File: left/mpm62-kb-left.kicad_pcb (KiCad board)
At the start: 2 copper layers, 138.1 x 95.2 mm, 65 parts, among them J1 Conn_01x04_Male, SW1 SW_Push, U1 ProMicro

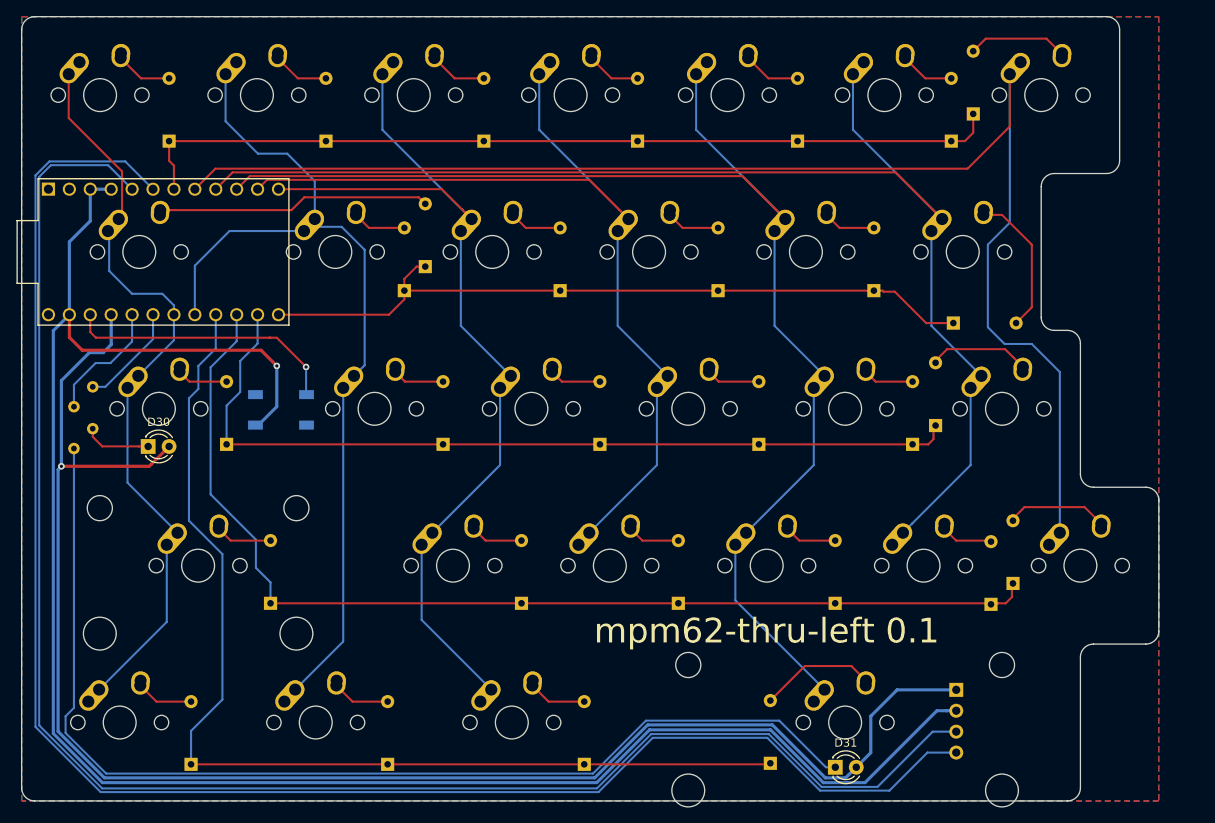
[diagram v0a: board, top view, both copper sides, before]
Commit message: Fix issues with left side: 1. SCL and SDA are swapped in the library file from github/ProMicroKiCad. Current fix is to swap the wires and mark the schematic to show which is which. Ultimately it would be good to get an updated lib file, but there is a PR for this which has never been accepted. 2. Was missing pullup resistors for I2C bus. 3. Resistor sizes on PCB were smaller than typical TH resistors. 4. Added extra header for power and ground to ease debugging.
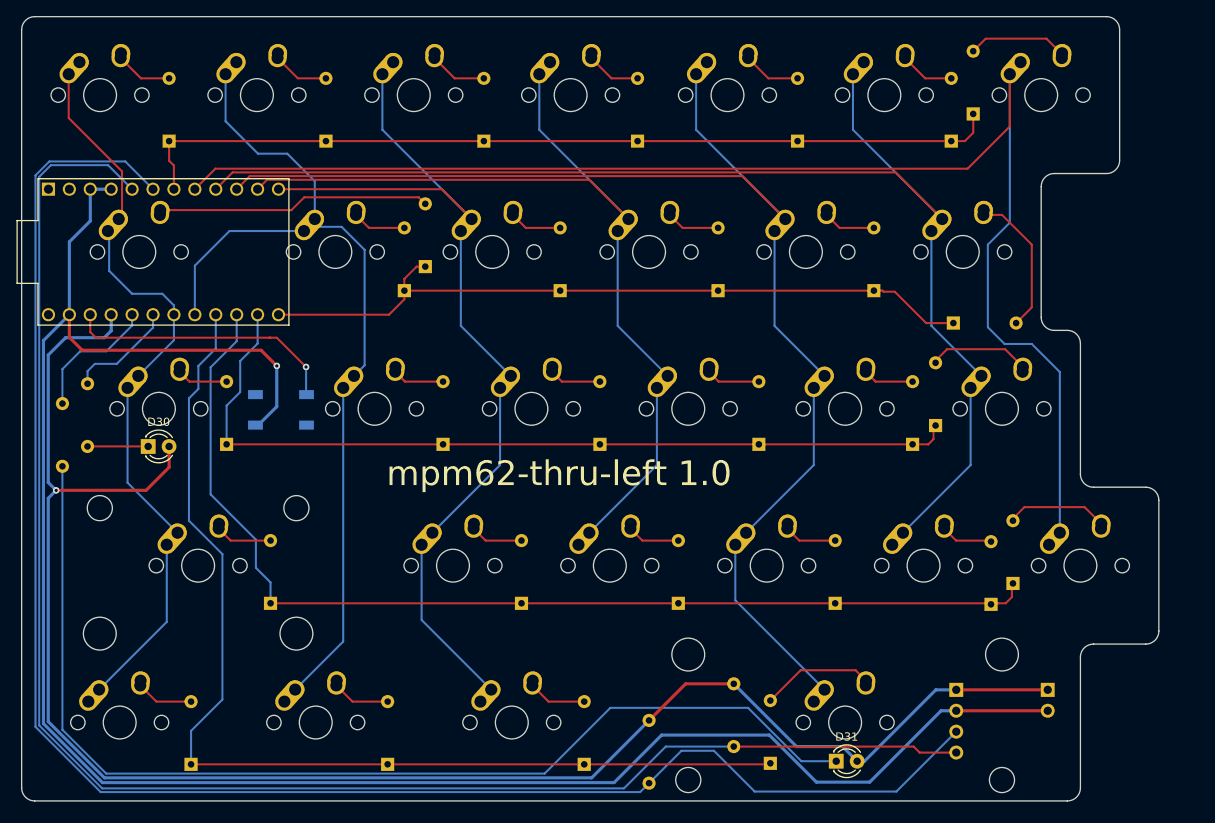
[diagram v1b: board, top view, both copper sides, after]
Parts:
- added J2: Conn_01x02_Male, Connector_PinHeader_2.54mm:PinHeader_1x02_P2.54mm_Vertical, B.Cu at (204.0, 113.5)
- added R3: 2.2K, Resistor_THT:R_Axial_DIN0207_L6.3mm_D2.5mm_P7.62mm_Horizontal, B.Cu at (165.9, 112.8)
- added R4: 2.2K, Resistor_THT:R_Axial_DIN0207_L6.3mm_D2.5mm_P7.62mm_Horizontal, B.Cu at (155.6, 117.2)
- MX23: footprint MX_Alps_Hybrid:MX-3U-NoLED -> MX_Alps_Hybrid:MX-3U-ReversedStabilizers-NoLED
- R1, R2: value R_Small -> 100; footprint Resistor_THT:R_Axial_DIN0204_L3.6mm_D1.6mm_P5.08mm_Horizontal -> Resistor_THT:R_Axial_DIN0207_L6.3mm_D2.5mm_P7.62mm_Horizontal
- moved R2 2.57 mm to (84.3, 86.4)
- moved R1 2.25 mm to (87.4, 83.9)
- moved D31 0.74 mm to (178.3, 122.2)
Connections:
- U1 pad 5: Net-(J1-Pad3) -> Net-(J1-Pad4)
- U1 pad 6: Net-(J1-Pad4) -> Net-(J1-Pad3)
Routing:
- net VCC: track 192.1 -> 210.0 mm
- net GND: track 229.4 -> 240.9 mm
- net Net-(J1-Pad4): track 205.8 -> 197.2 mm
- net Net-(J1-Pad3): track 202.4 -> 205.6 mm
- net Net-(D31-Pad1): track 135.5 -> 134.2 mm
- net Net-(R2-Pad2): track 15.2 -> 16.2 mm
- net Net-(D30-Pad1): track 8.21 -> 7.37 mm
- net Net-(R1-Pad2): track 12.7 -> 13.2 mm
- removed copper zone on B.Cu, net GND
- removed copper zone on F.Cu, net GND
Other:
- board text added: "mpm62-thru-left 1.0"
- board text removed: "mpm62-thru-left 0.1"

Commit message: Final for b1t (board 1 thruhole) board
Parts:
- added G***: LOGO, MpmMisc:small_logo, B.Cu at (121.4, 108.7)
- added G***: LOGO, MpmMisc:biglogo3, F.Cu at (144.4, 73.9)
- added H1: MountingHole, MountingHole:MountingHole_2.2mm_M2_Pad, F.Cu at (105.6, 60.3)
- added H2: MountingHole, MountingHole:MountingHole_2.2mm_M2_Pad, F.Cu at (103.2, 117.5)
- added H3: MountingHole, MountingHole:MountingHole_2.2mm_M2_Pad, F.Cu at (193.7, 50.8)
- added H4: MountingHole, MountingHole:MountingHole_2.2mm_M2_Pad, F.Cu at (192.9, 110.3)
- added U2: TRRS, Keebio-Parts:TRRS-PJ-320A, B.Cu at (204.3, 113.7)
- J1: value Conn_01x04_Male -> Raw Header
- J2: value Conn_01x02_Male -> JST ZH header; footprint Connector_PinHeader_2.54mm:PinHeader_1x02_P2.54mm_Vertical -> MpmMisc:JST_ZH_B4B-ZR_1x04_P1.50mm_Vertical
- MX1, MX10, MX11, MX12, MX13, MX15, MX16, MX17, MX18, MX19, MX20, MX21, MX22, MX24, MX25, MX26, MX27, MX28, MX29, MX6, MX7, MX8: footprint MX_Alps_Hybrid:MX-1U-NoLED -> MX_Only:MXOnly-1U-NoLED
- MX14, MX5, MX9: footprint MX_Alps_Hybrid:MX-1.25U-NoLED -> MX_Only:MXOnly-1.25U-NoLED
- MX2: footprint MX_Alps_Hybrid:MX-1.5U-NoLED -> MX_Only:MXOnly-1.5U-NoLED
- MX23: footprint MX_Alps_Hybrid:MX-3U-ReversedStabilizers-NoLED -> MX_Only:MXOnly-3U-ReversedStabilizers-NoLED
- MX3: footprint MX_Alps_Hybrid:MX-1.75U-NoLED -> MX_Only:MXOnly-1.75U-NoLED
- MX4: footprint MX_Alps_Hybrid:MX-2.25U-NoLED -> MX_Only:MXOnly-2.25U-NoLED
- moved R2 90.7 mm to (166.8, 124.3)
- moved U1 60.8 mm to (154.4, 79.2), turned to 180 degrees
- moved D2 26.8 mm to (101.7, 65.0)
- moved D17 17.7 mm to (180.2, 70.1), turned to 180 degrees
- moved D18 16.7 mm to (142.6, 100.6)
- moved D12 16.5 mm to (133.2, 81.5)
- moved R4 12.6 mm to (158.9, 105.0), turned to 90 degrees
- moved J2 11.7 mm to (192.4, 115.4), turned to 270 degrees
- moved D25 9.53 mm to (185.5, 62.5), turned to 90 degrees
- moved R1 9.16 mm to (95.0, 89.0), turned to 0 degrees
- moved R3 8.69 mm to (161.9, 105.0), turned to 90 degrees
- moved J1 4.31 mm to (188.6, 113.9)
- moved D5 0.65 mm to (99.3, 122.4)
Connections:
- U1 pad 10: COL4 -> Net-(R1-Pad2)
- U1 pad 11: COL3 -> COL1
- U1 pad 12: COL2 -> COL0
- U1 pad 13: ROW1 -> COL2
- U1 pad 14: ROW2 -> COL3
- U1 pad 15: ROW3 -> COL4
- U1 pad 16: ROW4 -> COL5
- U1 pad 17: COL1 -> COL6
- U1 pad 18: COL0 -> ROW2
- U1 pad 19: Net-(R1-Pad2) -> ROW1
- U1 pad 20: Net-(R2-Pad2) -> ROW0
- U1 pad 7: ROW0 -> Net-(R2-Pad2)
- U1 pad 8: COL6 -> ROW3
- U1 pad 9: COL5 -> ROW4
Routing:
- net Net-(J1-Pad3): track 205.6 -> 67.7 mm, vias 0 -> 1
- net Net-(J1-Pad4): track 197.2 -> 66.4 mm
- net Net-(D31-Pad1): track 134.2 -> 12.5 mm
- net GND: track 240.9 -> 158.7 mm
- net COL0: track 88.4 -> 132.3 mm
- net COL4: track 154.7 -> 117.4 mm, vias 0 -> 1
- net COL5: track 154.6 -> 117.8 mm
- net COL3: track 112.7 -> 80.5 mm
- net Net-(R1-Pad2): track 13.2 -> 45.1 mm
- net Net-(D2-Pad2): track 33.5 -> 6.67 mm
- net COL6: track 172.8 -> 147.5 mm
- net Net-(SW1-Pad1): track 33.6 -> 57.9 mm, vias 1 -> 0
- net Net-(R2-Pad2): track 16.2 -> 38.4 mm
- net ROW4: track 129.6 -> 108.9 mm
- net ROW0: track 106.5 -> 126.1 mm
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- added copper zone on B.Cu, net GND
- added copper zone on F.Cu, net GND
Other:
- board text added: "minke·io b1t-left 1.0"
- board text removed: "mpm62-thru-left 1.0"
